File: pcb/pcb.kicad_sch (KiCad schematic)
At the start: 20 parts, among them J1 Screw_Terminal_01x02, J2 Conn_01x04_Pin, J3 Screw_Terminal_01x03, J4 Screw_Terminal_01x03, J5 Screw_Terminal_01x02, J6 Screw_Terminal_01x02, J7 Screw_Terminal_01x02, J8 Screw_Terminal_01x07, K1 SANYOU_SRD_Form_A, Q1 AO3400A, U1 AMS1117-3.3, U2 ESP32-C6-MINI-1

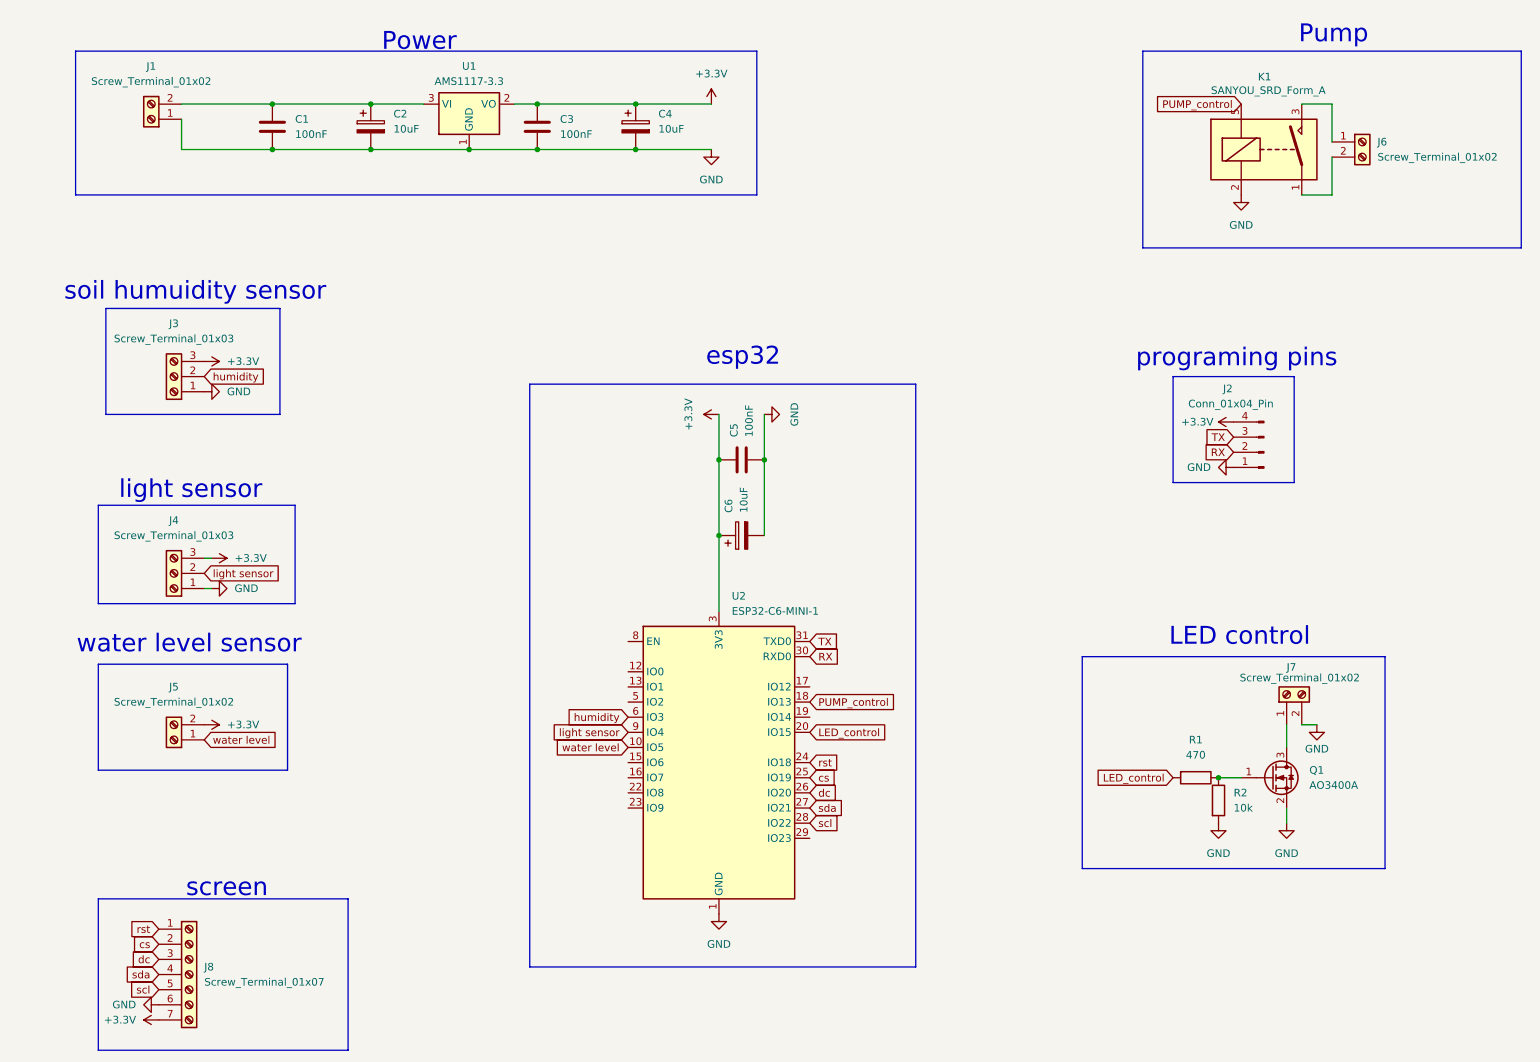
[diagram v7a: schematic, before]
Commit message: makin the shematic hirearhic
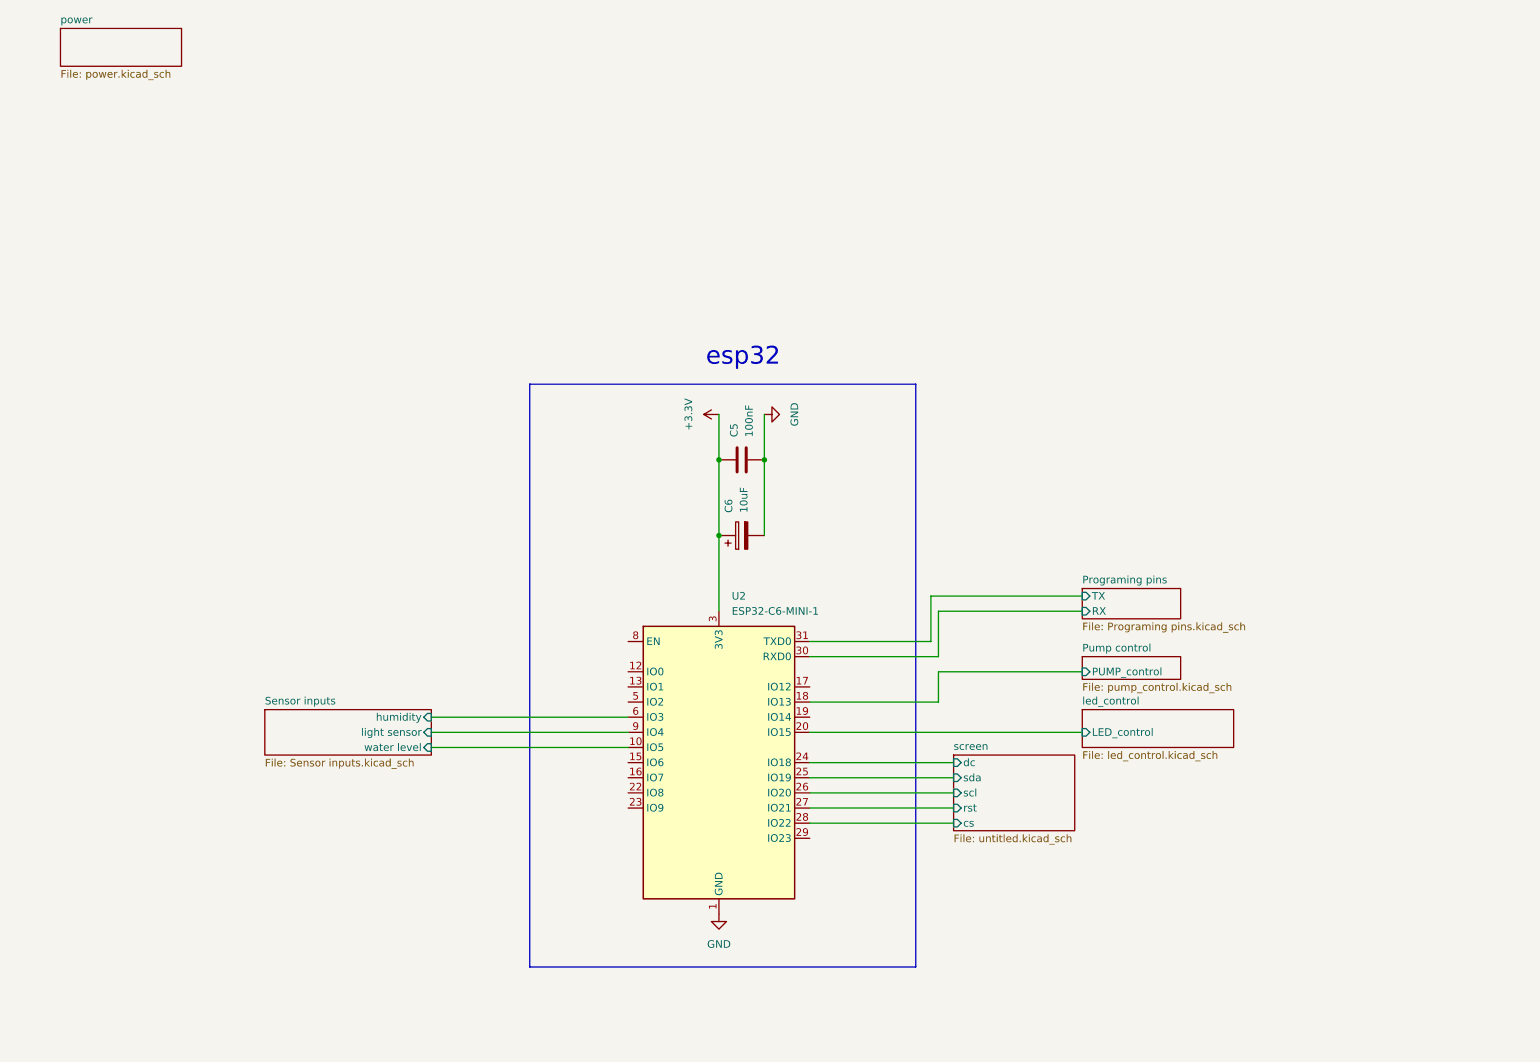
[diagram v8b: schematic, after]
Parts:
- removed C1, C3: 100nF, symbol Device:C
- removed C2, C4: 10uF, symbol Device:C_Polarized
- removed J1, J5, J6, J7: Screw_Terminal_01x02, symbol Connector:Screw_Terminal_01x02
- removed J2: Conn_01x04_Pin, Connector_PinSocket_2.54mm:PinSocket_1x04_P2.54mm_Vertical, symbol Connector:Conn_01x04_Pin
- removed J3, J4: Screw_Terminal_01x03, symbol Connector:Screw_Terminal_01x03
- removed J8: Screw_Terminal_01x07, symbol Connector:Screw_Terminal_01x07
- removed K1: SANYOU_SRD_Form_A, Relay_THT:Relay_SPST_SANYOU_SRD_Series_Form_A, symbol Relay:SANYOU_SRD_Form_A
- removed Q1: AO3400A, Package_TO_SOT_SMD:SOT-23, symbol Transistor_FET:AO3400A
- removed R1: 470, symbol Device:R
- removed R2: 10k, symbol Device:R
- removed U1: AMS1117-3.3, Package_TO_SOT_SMD:SOT-223-3_TabPin2, symbol Regulator_Linear:AMS1117-3.3
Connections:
- net LED_control renamed led_control/LED_control
- net PUMP_control renamed Pump control/PUMP_control
- net RX renamed Programing pins/RX
- net TX renamed Programing pins/TX
- net cs renamed screen/sda
- net dc renamed screen/scl
- net humidity renamed Sensor inputs/humidity
- net light sensor renamed Sensor inputs/light sensor
- net rst renamed screen/dc
- net scl renamed screen/cs
- net sda renamed screen/rst
- net water level renamed Sensor inputs/water level
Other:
- added sheet Programing pins (Programing pins.kicad_sch)
- added sheet Pump control (pump_control.kicad_sch)
- added sheet Sensor inputs (Sensor inputs.kicad_sch)
- added sheet led_control (led_control.kicad_sch)
- added sheet power (power.kicad_sch)
- added sheet screen (untitled.kicad_sch)
- note removed: "LED control"
- note removed: "Power"
- note removed: "Pump"
- note removed: "light sensor"
- note removed: "programing pins"
- note removed: "screen"
- note removed: "soil humuidity sensor"
- note removed: "water level sensor"
